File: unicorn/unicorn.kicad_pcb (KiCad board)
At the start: 2 copper layers, 35 x 75 mm, 26 parts, among them J0 Conn_01x02, J1 Conn_01x14_Female, J2 Conn_01x14_Female, J3 SPI, U1 ATmega328-P, U2 L7805

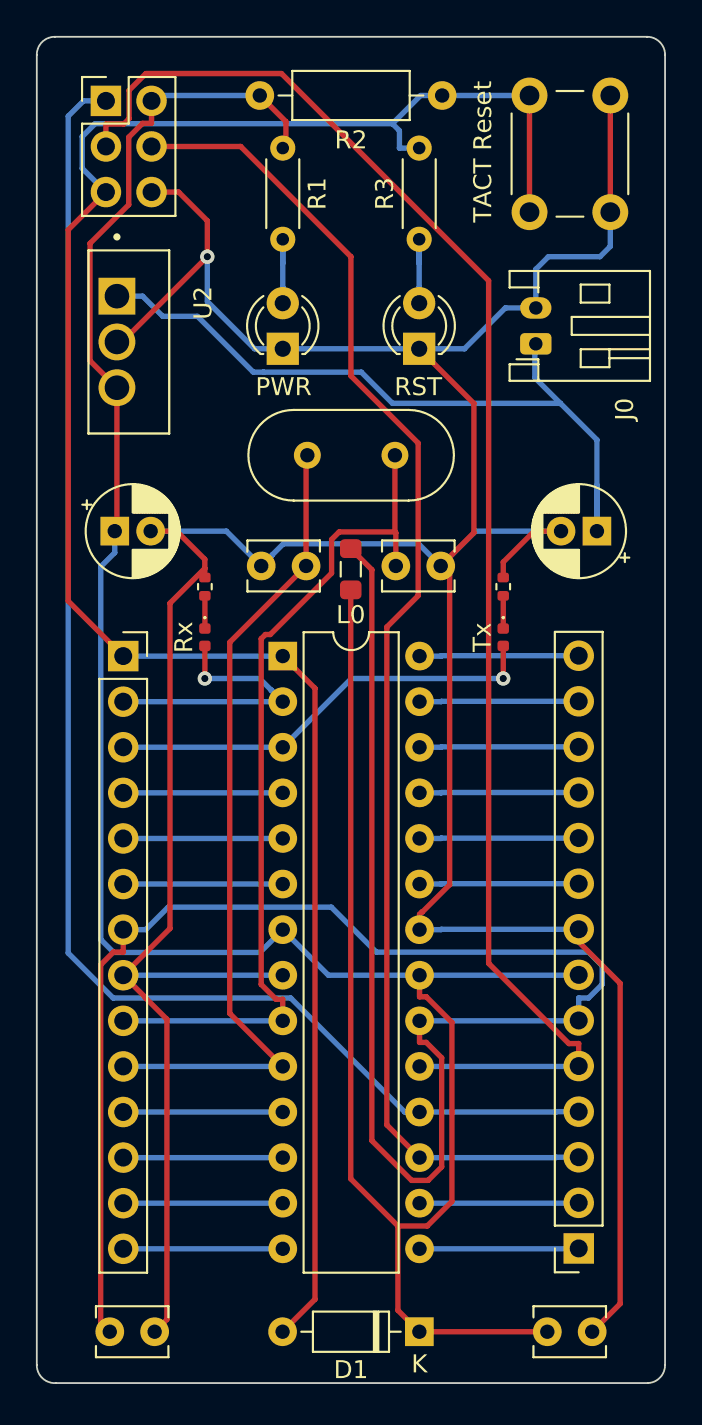
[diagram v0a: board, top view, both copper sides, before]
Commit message: Unicorn - Feat/fix components (#2)
* replace power connector
- still need to redo routing

* fix routing + replace power connector with the right one

* add jst connector + update step file
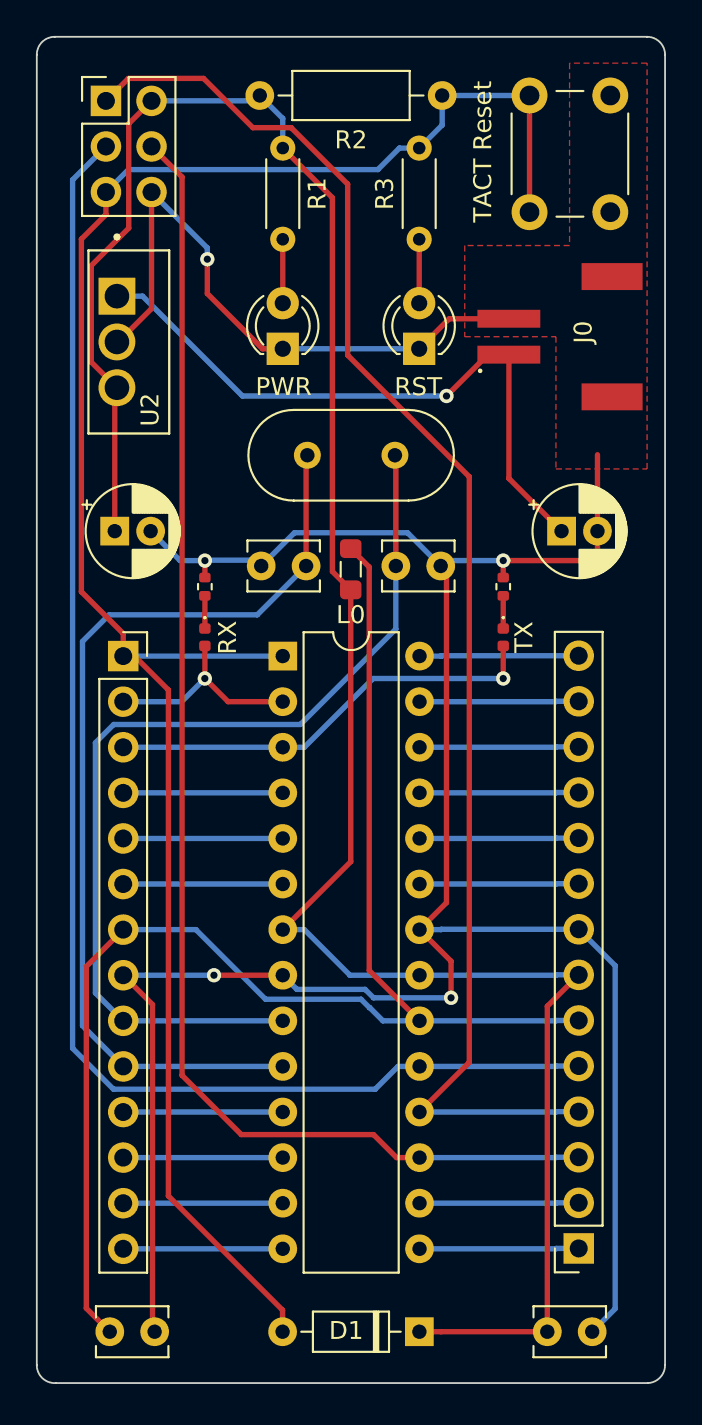
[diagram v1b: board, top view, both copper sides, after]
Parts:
- J0: footprint Connector_JST:JST_PH_S2B-PH-K_1x02_P2.00mm_Horizontal -> JST_S2B-PH-SM4-TB:JST_S2B-PH-SM4-TB
- LED3: value Tx -> TX
- LED4: value Rx -> RX
- moved C1 1.97 mm to (154.0, 87.5), turned to 0 degrees
- moved J0 1.55 mm to (151.0, 76.7), turned to -90 degrees
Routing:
- net GND: track 209.5 -> 167.3 mm, vias 1 -> 5
- net Net-(J1-Pin_6): track 112.2 -> 79.2 mm
- net Net-(D1-K): track 155.0 -> 127.6 mm
- net Net-(J2-Pin_10): track 46.0 -> 53.9 mm
- net Net-(J2-Pin_9): track 48.1 -> 55.0 mm
- net Net-(J0-Pin_1): track 41.6 -> 36.1 mm, vias 0 -> 1
- net Net-(J2-Pin_2): track 16.5 -> 11.8 mm
- net Net-(J1-Pin_5): track 84.5 -> 80.7 mm
- net Net-(D1-A): track 114.6 -> 111.2 mm
- net Net-(LED2-A): track 5.79 -> 3.56 mm
- net Net-(LED1-A): track 5.79 -> 3.56 mm
- net Net-(J1-Pin_3): track 75.7 -> 76.5 mm
- added copper zone on F.Cu, net GND
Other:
- board text added: "Unicorn rev_B"
- board text removed: "First sgiraz pcb"
